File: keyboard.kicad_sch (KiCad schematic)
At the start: 0 parts

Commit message: keyboard schematic update
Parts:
- added D1, D10, D11, D12, D13, D14, D15, D16, D17, D18, D19, D2, D20, D21, D22, D23, D24, D25, D26, D27, D28, D29, D3, D30, D31, D32, D33, D34, D35, D36, D37, D38, D39, D4, D40, D41, D42, D43, D44, D45, D46, D47, D5, D6, D7, D8, D9: 1N4148, Diode_THT:D_DO-35_SOD27_P7.62mm_Horizontal, symbol Diode:1N4148
- added SW1: ESC, symbol Switch:SW_MEC_5G
- added SW10: o, symbol Switch:SW_MEC_5G
- added SW11: p, symbol Switch:SW_MEC_5G
- added SW12: [, symbol Switch:SW_MEC_5G
- added SW13: ], symbol Switch:SW_MEC_5G
- added SW14: DEL, symbol Switch:SW_MEC_5G
- added SW15: FN, symbol Switch:SW_MEC_5G
- added SW16: a, symbol Switch:SW_MEC_5G
- added SW17: s, symbol Switch:SW_MEC_5G
- added SW18: d, symbol Switch:SW_MEC_5G
- added SW19: f, symbol Switch:SW_MEC_5G
- added SW2: q, symbol Switch:SW_MEC_5G
- added SW20: g, symbol Switch:SW_MEC_5G
- added SW21: h, symbol Switch:SW_MEC_5G
- added SW22: j, symbol Switch:SW_MEC_5G
- added SW23: k, symbol Switch:SW_MEC_5G
- added SW24: l, symbol Switch:SW_MEC_5G
- added SW25: ;, symbol Switch:SW_MEC_5G
- added SW26: ', symbol Switch:SW_MEC_5G
- added SW27: ENTER, symbol Switch:SW_MEC_5G
- added SW28: SHIFT, symbol Switch:SW_MEC_5G
- added SW29: z, symbol Switch:SW_MEC_5G
- added SW3: w, symbol Switch:SW_MEC_5G
- added SW30: x, symbol Switch:SW_MEC_5G
- added SW31: c, symbol Switch:SW_MEC_5G
- added SW32: v, symbol Switch:SW_MEC_5G
- added SW33: b, symbol Switch:SW_MEC_5G
- added SW34: n, symbol Switch:SW_MEC_5G
- added SW35: m, symbol Switch:SW_MEC_5G
- added SW36: ,, symbol Switch:SW_MEC_5G
- added SW37: ., symbol Switch:SW_MEC_5G
- added SW38: /, symbol Switch:SW_MEC_5G
- added SW39: UP, symbol Switch:SW_MEC_5G
- added SW4: e, symbol Switch:SW_MEC_5G
- added SW40: \, symbol Switch:SW_MEC_5G
- added SW41: CTRL, symbol Switch:SW_MEC_5G
- added SW42: ALT, symbol Switch:SW_MEC_5G
- added SW43: SPACE, symbol Switch:SW_MEC_5G
- added SW44: SUPER, symbol Switch:SW_MEC_5G
- added SW45: LEFT, symbol Switch:SW_MEC_5G
- added SW46: DOWN, symbol Switch:SW_MEC_5G
- added SW47: RIGHT, symbol Switch:SW_MEC_5G
- added SW5: r, symbol Switch:SW_MEC_5G
- added SW6: t, symbol Switch:SW_MEC_5G
- added SW7: y, symbol Switch:SW_MEC_5G
- added SW8: u, symbol Switch:SW_MEC_5G
- added SW9: i, symbol Switch:SW_MEC_5G
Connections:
- new net: D15.2 (A), SW15.3 (B), SW15.4 (B)
- new net: D9.2 (A), SW9.3 (B), SW9.4 (B)
- new net: D36.2 (A), SW36.3 (B), SW36.4 (B)
- new net: D20.2 (A), SW20.3 (B), SW20.4 (B)
- new net: D24.2 (A), SW24.3 (B), SW24.4 (B)
- new net: D45.2 (A), SW45.3 (B), SW45.4 (B)
- new net: D38.2 (A), SW38.3 (B), SW38.4 (B)
- new net: D19.2 (A), SW19.3 (B), SW19.4 (B)
- new net: D12.2 (A), SW12.3 (B), SW12.4 (B)
- new net: D39.2 (A), SW39.3 (B), SW39.4 (B)
- new net: D33.2 (A), SW33.3 (B), SW33.4 (B)
- new net: D7.2 (A), SW7.3 (B), SW7.4 (B)
- new net: D14.2 (A), SW14.3 (B), SW14.4 (B)
- new net: D18.2 (A), SW18.3 (B), SW18.4 (B)
- new net: D34.2 (A), SW34.3 (B), SW34.4 (B)
- new net: D31.2 (A), SW31.3 (B), SW31.4 (B)
- new net: D22.2 (A), SW22.3 (B), SW22.4 (B)
- new net: D30.2 (A), SW30.3 (B), SW30.4 (B)
- new net: D26.2 (A), SW26.3 (B), SW26.4 (B)
- new net: D5.2 (A), SW5.3 (B), SW5.4 (B)
- new net: D44.2 (A), SW44.3 (B), SW44.4 (B)
- new net: D2.2 (A), SW2.3 (B), SW2.4 (B)
- new net: D37.2 (A), SW37.3 (B), SW37.4 (B)
- new net: D3.2 (A), SW3.3 (B), SW3.4 (B)
- new net: D6.2 (A), SW6.3 (B), SW6.4 (B)
- new net: D17.2 (A), SW17.3 (B), SW17.4 (B)
- new net: D40.2 (A), SW40.3 (B), SW40.4 (B)
- new net: D28.2 (A), SW28.3 (B), SW28.4 (B)
- new net: D11.2 (A), SW11.3 (B), SW11.4 (B)
- new net: D10.2 (A), SW10.3 (B), SW10.4 (B)
- new net: D4.2 (A), SW4.3 (B), SW4.4 (B)
- new net: D32.2 (A), SW32.3 (B), SW32.4 (B)
- new net: D27.2 (A), SW27.3 (B), SW27.4 (B)
- new net: D41.2 (A), SW41.3 (B), SW41.4 (B)
- new net: D1.2 (A), SW1.3 (B), SW1.4 (B)
- new net: D47.2 (A), SW47.3 (B), SW47.4 (B)
- new net: D35.2 (A), SW35.3 (B), SW35.4 (B)
- new net: D13.2 (A), SW13.3 (B), SW13.4 (B)
- new net: D21.2 (A), SW21.3 (B), SW21.4 (B)
- new net: D43.2 (A), SW43.3 (B), SW43.4 (B)
- new net: D16.2 (A), SW16.3 (B), SW16.4 (B)
- new net: D46.2 (A), SW46.3 (B), SW46.4 (B)
- new net: D29.2 (A), SW29.3 (B), SW29.4 (B)
- new net: D23.2 (A), SW23.3 (B), SW23.4 (B)
- new net: D8.2 (A), SW8.3 (B), SW8.4 (B)
- new net: D25.2 (A), SW25.3 (B), SW25.4 (B)
- new net: D42.2 (A), SW42.3 (B), SW42.4 (B)
- new net Col1: SW1.1 (A), SW1.2 (A), SW15.1 (A), SW15.2 (A), SW28.1 (A), SW28.2 (A), SW41.1 (A), SW41.2 (A)
- new net Col10: SW10.1 (A), SW10.2 (A), SW24.1 (A), SW24.2 (A), SW37.1 (A), SW37.2 (A), SW44.1 (A), SW44.2 (A)
- new net Col11: SW11.1 (A), SW11.2 (A), SW25.1 (A), SW25.2 (A), SW38.1 (A), SW38.2 (A), SW45.1 (A), SW45.2 (A)
- new net Col12: SW12.1 (A), SW12.2 (A), SW26.1 (A), SW26.2 (A), SW39.1 (A), SW39.2 (A), SW46.1 (A), SW46.2 (A)
- new net Col13: SW13.1 (A), SW13.2 (A), SW27.1 (A), SW27.2 (A), SW40.1 (A), SW40.2 (A), SW47.1 (A), SW47.2 (A)
- new net Col14: SW14.1 (A), SW14.2 (A)
- new net Col2: SW16.1 (A), SW16.2 (A), SW2.1 (A), SW2.2 (A), SW29.1 (A), SW29.2 (A), SW42.1 (A), SW42.2 (A)
- new net Col3: SW17.1 (A), SW17.2 (A), SW3.1 (A), SW3.2 (A), SW30.1 (A), SW30.2 (A)
- new net Col4: SW18.1 (A), SW18.2 (A), SW31.1 (A), SW31.2 (A), SW4.1 (A), SW4.2 (A)
- new net Col5: SW19.1 (A), SW19.2 (A), SW32.1 (A), SW32.2 (A), SW5.1 (A), SW5.2 (A)
- new net Col6: SW20.1 (A), SW20.2 (A), SW33.1 (A), SW33.2 (A), SW43.1 (A), SW43.2 (A), SW6.1 (A), SW6.2 (A)
- new net Col7: SW21.1 (A), SW21.2 (A), SW34.1 (A), SW34.2 (A), SW7.1 (A), SW7.2 (A)
- new net Col8: SW22.1 (A), SW22.2 (A), SW35.1 (A), SW35.2 (A), SW8.1 (A), SW8.2 (A)
- new net Col9: SW23.1 (A), SW23.2 (A), SW36.1 (A), SW36.2 (A), SW9.1 (A), SW9.2 (A)
- new net Row1: D1.1 (K), D10.1 (K), D11.1 (K), D12.1 (K), D13.1 (K), D14.1 (K), D2.1 (K), D3.1 (K), D4.1 (K), D5.1 (K), D6.1 (K), D7.1 (K), D8.1 (K), D9.1 (K)
- new net Row2: D15.1 (K), D16.1 (K), D17.1 (K), D18.1 (K), D19.1 (K), D20.1 (K), D21.1 (K), D22.1 (K), D23.1 (K), D24.1 (K), D25.1 (K), D26.1 (K), D27.1 (K)
- new net Row3: D28.1 (K), D29.1 (K), D30.1 (K), D31.1 (K), D32.1 (K), D33.1 (K), D34.1 (K), D35.1 (K), D36.1 (K), D37.1 (K), D38.1 (K), D39.1 (K), D40.1 (K)
- new net Row4: D41.1 (K), D42.1 (K), D43.1 (K), D44.1 (K), D45.1 (K), D46.1 (K), D47.1 (K)

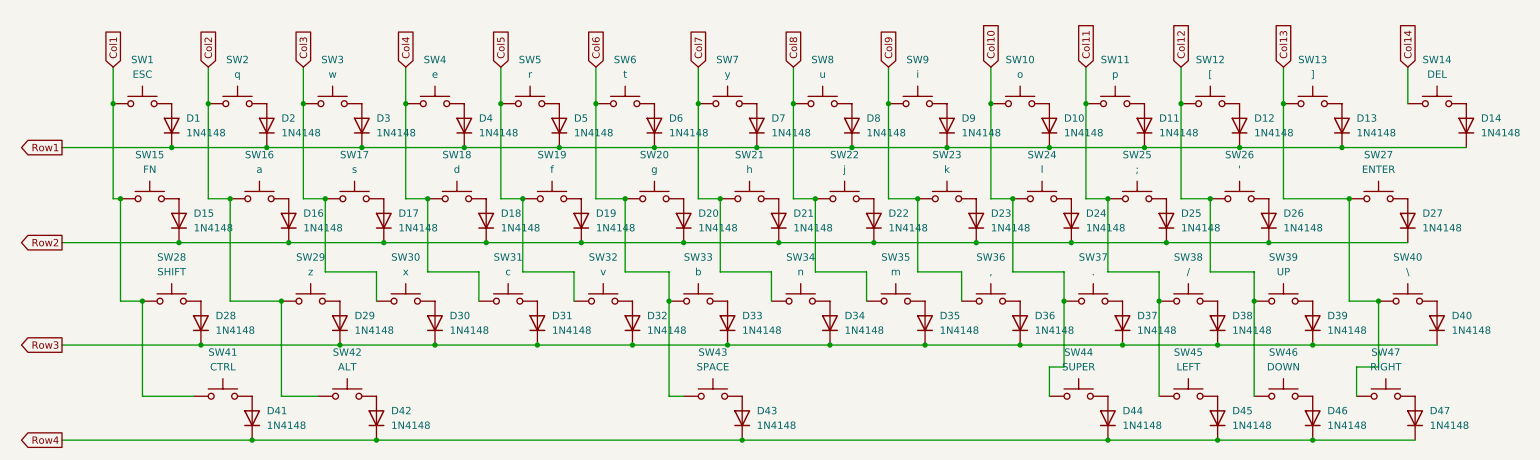
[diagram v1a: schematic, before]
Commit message: mostly done schematic
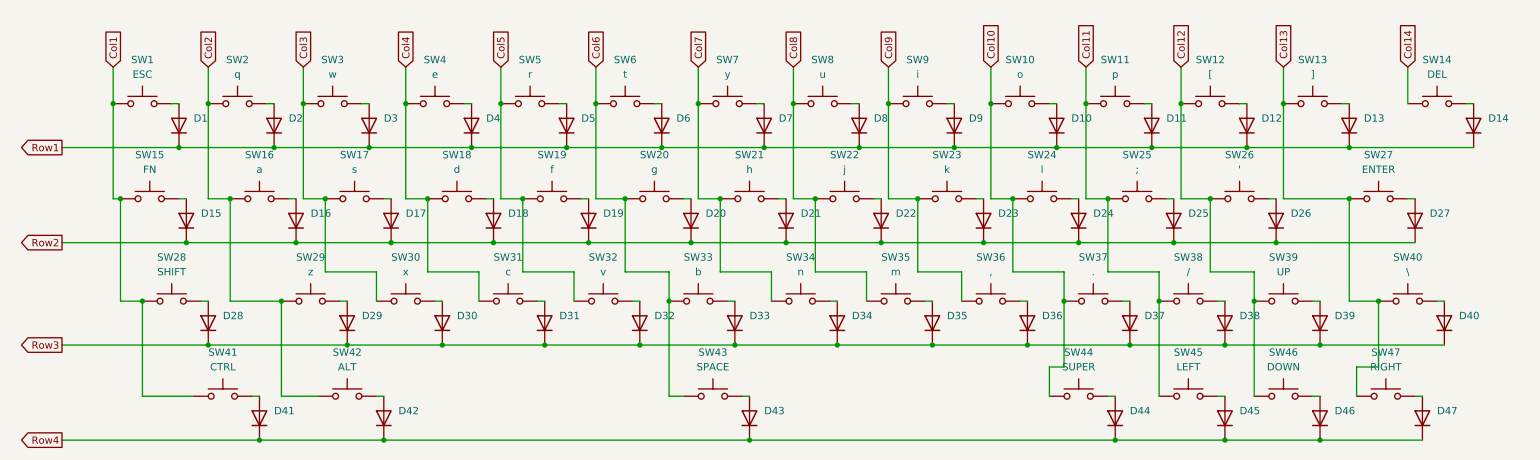
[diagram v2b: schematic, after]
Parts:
- SW1, SW10, SW11, SW12, SW13, SW14, SW16, SW17, SW18, SW19, SW2, SW20, SW21, SW22, SW23, SW24, SW25, SW26, SW29, SW3, SW30, SW31, SW32, SW33, SW34, SW35, SW36, SW37, SW38, SW39, SW4, SW45, SW46, SW47, SW5, SW6, SW7, SW8, SW9: footprint (none) -> Button_Switch_Keyboard:SW_Cherry_MX_1.00u_PCB
- SW15, SW41, SW42, SW44: footprint (none) -> Button_Switch_Keyboard:SW_Cherry_MX_1.25u_PCB
- SW27: footprint (none) -> Button_Switch_Keyboard:SW_Cherry_MX_2.00u_PCB
- SW28: footprint (none) -> Button_Switch_Keyboard:SW_Cherry_MX_1.75u_PCB
- SW40: footprint (none) -> Button_Switch_Keyboard:SW_Cherry_MX_1.50u_PCB
- SW43: footprint (none) -> Button_Switch_Keyboard:SW_Cherry_MX_6.25u_PCB
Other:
- moved on the sheet: D1, D10, D11, D12, D13, D14, D15, D16, D17, D18, D19, D2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
